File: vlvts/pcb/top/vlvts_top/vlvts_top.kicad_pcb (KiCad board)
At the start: 2 copper layers, 46 x 46 mm, 52 parts, among them J2 Conn_01x14_Male, Q1 YJL2305A-YAN, Q2 YJL2305A-YAN, Q3 YJL2305A-YAN, U5 SCT2024CSSG

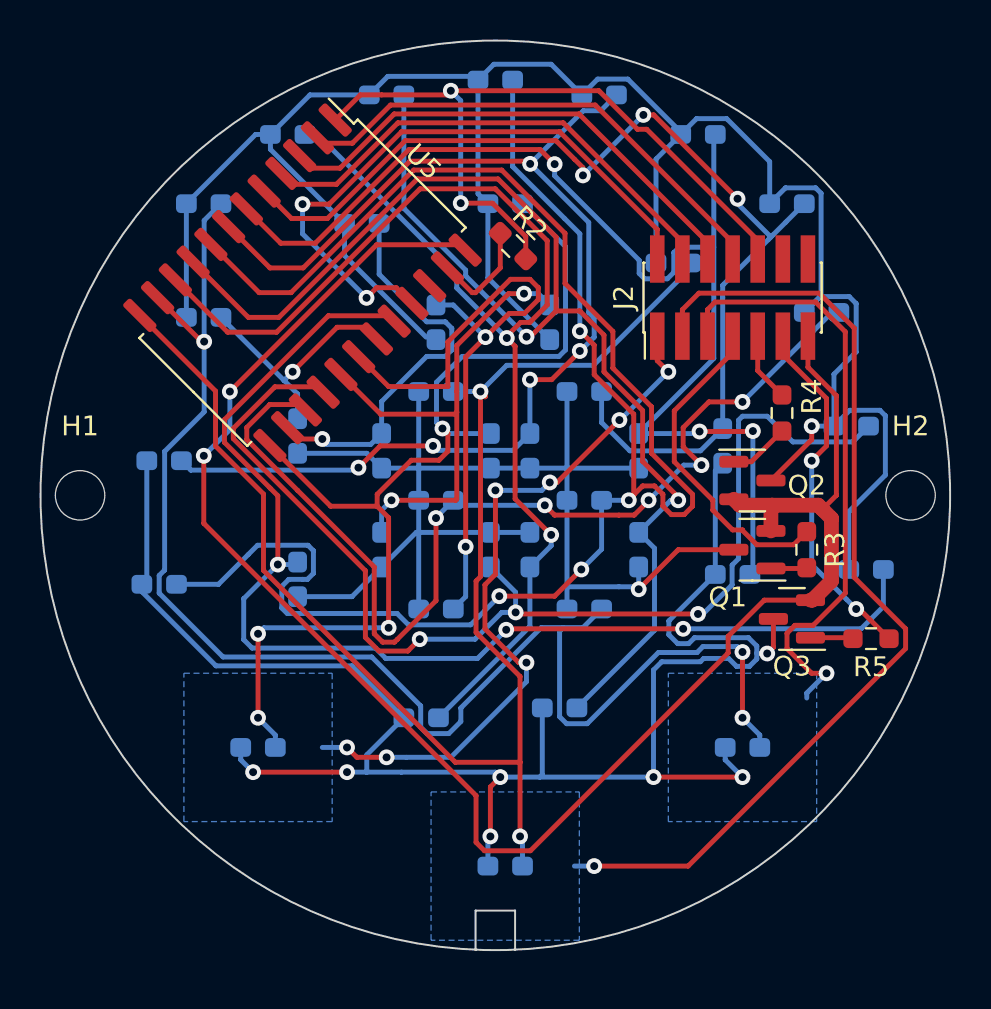
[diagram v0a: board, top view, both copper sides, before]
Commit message: vlvts: new pcb
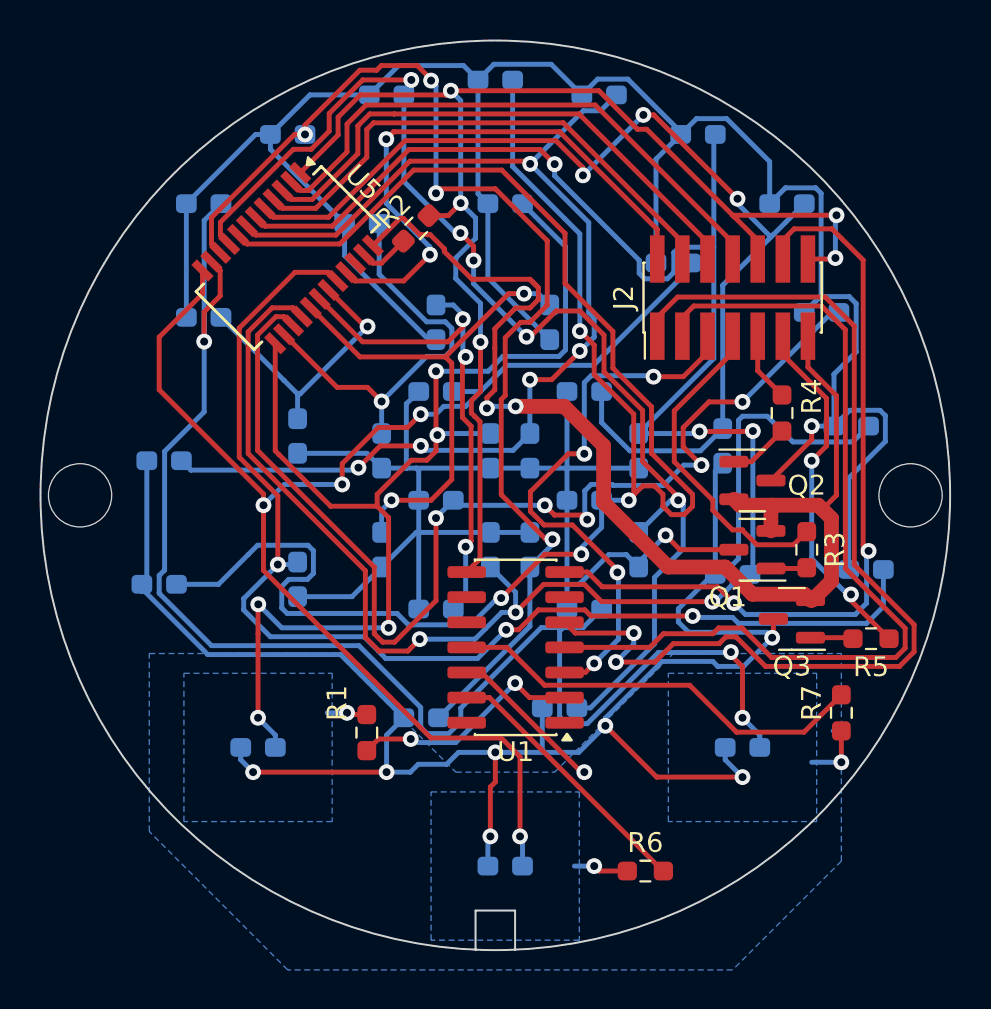
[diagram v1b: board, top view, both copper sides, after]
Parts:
- added R1: 1M, Resistor_SMD:R_0603_1608Metric_Pad0.98x0.95mm_HandSolder, F.Cu at (72.5, 112.0)
- added R6: 1M, Resistor_SMD:R_0603_1608Metric_Pad0.98x0.95mm_HandSolder, F.Cu at (86.6, 119.0)
- added R7: 1M, Resistor_SMD:R_0603_1608Metric_Pad0.98x0.95mm_HandSolder, F.Cu at (96.5, 111.0)
- added U1: CAP1296-1-SL, Package_SO:SOIC-14_3.9x8.7mm_P1.27mm, F.Cu at (80.0, 107.7)
- H1, H2: footprint MountingHole:MountingHole_2.5mm -> MountingHole:MountingHole_3.2mm_M3_DIN965; moved to B.Cu
- U5: footprint Package_SO:SOP-24_7.5x15.4mm_P1.27mm -> Package_SO:SSOP-24_3.9x8.7mm_P0.635mm
- moved R2 4.98 mm to (75.0, 86.5), turned to -135 degrees
- moved U5 1.46 mm to (68.5, 88.0)
- turned H1 to 180 degrees
- turned H2 to 180 degrees
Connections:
- J2 pad 1: BTN_L -> CAP_CLK
- J2 pad 3: BTN_C -> CAP_DATA
- J2 pad 5: BTN_R -> CAP_IRQ
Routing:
- net CAP_CLK: track 0.00 -> 51.8 mm, vias 0 -> 2
- net CAP_DATA: track 0.00 -> 45.7 mm
- net VDD: track 0.00 -> 40.2 mm, vias 0 -> 2
- net BTN_C: track 49.7 -> 13.6 mm, vias 1 -> 0
- net GND: track 37.1 -> 67.5 mm, vias 2 -> 5
- net CAP_IRQ: track 0.00 -> 28.4 mm, vias 0 -> 4
- net VEE: track 87.9 -> 61.6 mm
- net BTN_L: track 36.5 -> 11.9 mm, vias 7 -> 2
- net BTN_R: track 31.1 -> 21.6 mm, vias 1 -> 0
- net Net-(D20-K): track 70.5 -> 61.2 mm, vias 2 -> 5
- net Net-(D13-K): track 35.1 -> 26.0 mm, vias 2 -> 3
- net Net-(D21-K): track 67.4 -> 59.1 mm, vias 2 -> 4
- net BTN_SG: track 0.00 -> 8.04 mm, vias 0 -> 1
- net Net-(D24-K): track 52.8 -> 59.4 mm, vias 4 -> 5
- net Net-(D10-K): track 52.8 -> 57.3 mm
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- added copper zone on B.Cu, net /BTN_TCH_C
- added copper zone on B.Cu, net /BTN_TCH_L
- added copper zone on B.Cu, net /BTN_TCH_R
- added copper zone on B.Cu, net BTN_SG
- removed copper zone on B.Cu, net BTN_C
- removed copper zone on B.Cu, net BTN_L
- removed copper zone on B.Cu, net BTN_R
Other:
- board text added: "vlvts top 0.2 Hubert Miś 2025"
- board text removed: "vlvts top 0.1 Hubert Miś 2024"
